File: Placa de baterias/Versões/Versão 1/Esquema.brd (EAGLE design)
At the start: 41.9 x 28.6 mm, 7 parts

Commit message: teste
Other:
- board size 41.9 x 28.6 mm -> 41.9 x 27.9 mm
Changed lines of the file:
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@@
 </layers>
 <board>
-<fusionsync huburn="a.YnVzaW5lc3M6ZGlzY2VudGUxNzg" projecturn="a.YnVzaW5lc3M6ZGlzY2VudGUxNzgjRDIwMjIwNjExNTMyNjQzNTAx" f3durn="urn:adsk.wipprod:dm.lineage:PkS-i6vOSt6JP8FzX6P3mg" pcbguid="" lastpulledtime="" lastsyncedchangeguid="" latestrevisionid="dae5b02e-3f86-4753-98fb-deca12bab6cc" lastsyncedrevisionid="dae5b02e-3f86-4753-98fb-deca12bab6cc" lastboardhashguid="e1b1cba6-bc9d-dcd1-c240-c72e3c8944e4" lastpushedtime="2025-07-01T22:19:30Z" linktopcb3d="true"/>
+<fusionsync huburn="a.YnVzaW5lc3M6ZGlzY2VudGUxNzg" projecturn="a.YnVzaW5lc3M6ZGlzY2VudGUxNzgjRDIwMjIwNjExNTMyNjQzNTAx" f3durn="urn:adsk.wipprod:dm.lineage:Dvtrc6K0SWqyUMVJzSpTWQ" pcbguid="" lastpulledtime="" lastsyncedchangeguid="" latestrevisionid="de83ba8c-14a2-4f2c-87d4-37bcf2589fd9" lastsyncedrevisionid="de83ba8c-14a2-4f2c-87d4-37bcf2589fd9" lastboardhashguid="3ac31985-926d-b8f2-58d9-c6a5415b0390" lastpushedtime="2025-09-09T18:21:38Z" linktopcb3d="true"/>
 <plain>
 <hole x="39.37" y="15.24" drill="3"/>
@@
 <hole x="2.54" y="2.54" drill="3"/>
 <hole x="2.54" y="15.24" drill="3"/>
-<wire x1="41.91" y1="0" x2="41.91" y2="17.78" width="0" layer="20"/>
-<wire x1="0" y1="17.78" x2="41.91" y2="17.78" width="0" layer="20" curve="-108.924644"/>
-<wire x1="0" y1="17.78" x2="0" y2="0" width="0" layer="20"/>
+<wire x1="41.91" y1="0" x2="41.91" y2="17.145" width="0" layer="20"/>
+<wire x1="0" y1="17.145" x2="41.91" y2="17.145" width="0" layer="20" curve="-108.924644"/>
+<wire x1="0" y1="17.145" x2="0" y2="0" width="0" layer="20"/>
 <wire x1="0" y1="0" x2="41.91" y2="0" width="0" layer="20"/>
 <dimension x1="0" y1="-1.27" x2="41.91" y2="-1.27" x3="20.955" y3="-3.81" textsize="1.778" layer="27"/>

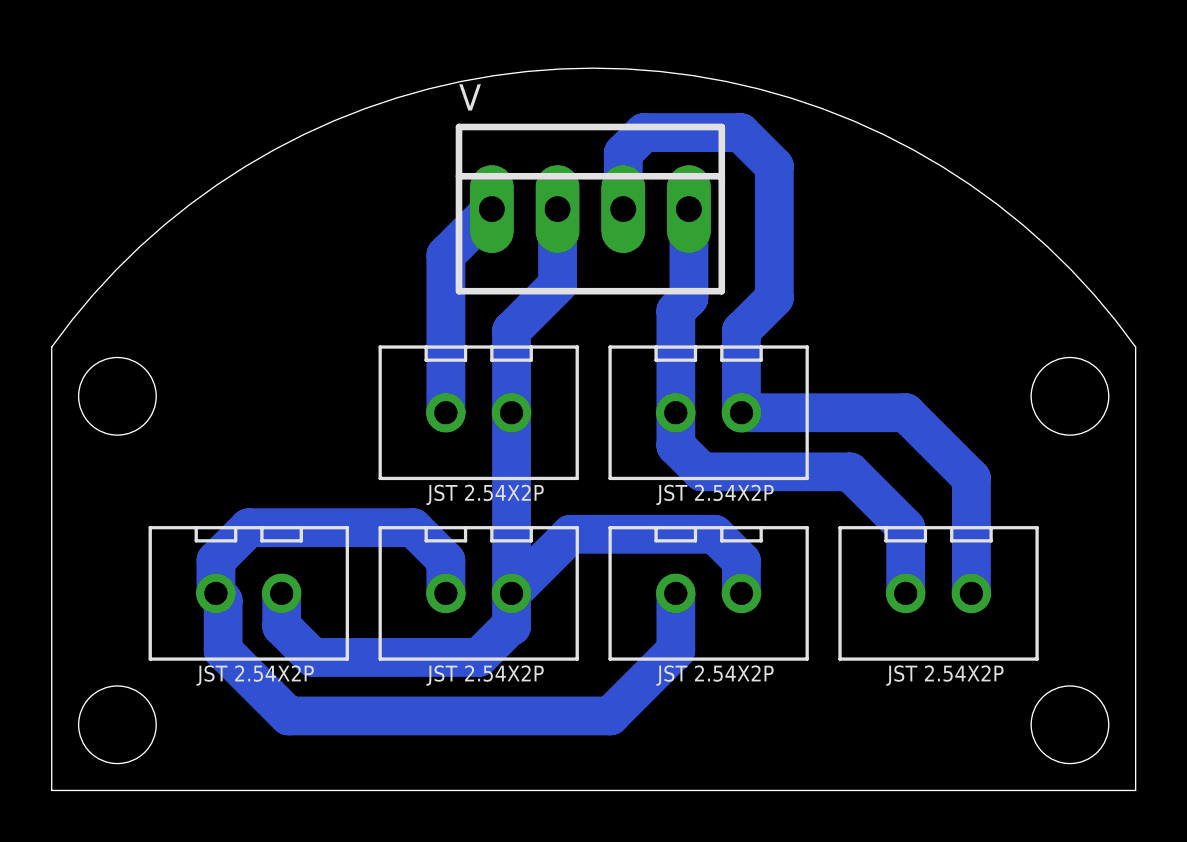
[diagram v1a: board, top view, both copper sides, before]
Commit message: CHORE: adicionando pads ovais na placa de processamento
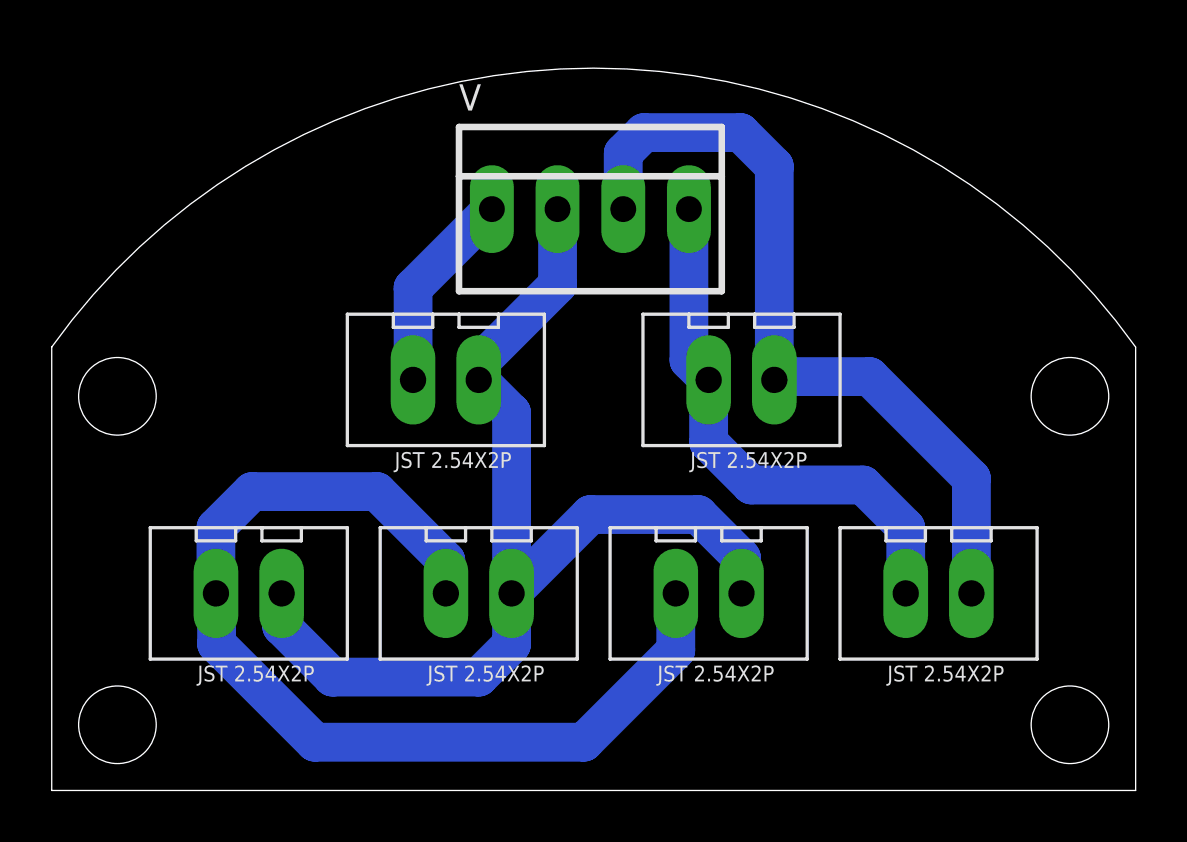
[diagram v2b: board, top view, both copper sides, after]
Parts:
- moved U$4 1.80 mm to (26.7, 15.9)
- moved U$5 1.80 mm to (15.2, 15.9)
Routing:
- net V2+: track 39.5 -> 42.3 mm
- net V1+: track 33.3 -> 30.9 mm
- net V2-: track 45.2 -> 47.2 mm
- net V1-: track 22.1 -> 20.9 mm
